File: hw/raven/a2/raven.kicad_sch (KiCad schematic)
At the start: 79 parts, among them J101 Pinhdr_01x02, J102 Pinhdr_01x03, J103 JTAG IN, J104 Pinhdr_01x03, J105 Pinhdr_01x03, SW101 SW_Push, U101 74LS148, U102 74AHC157, U103 SN74LVCH16245, U104 MC68150, U105 CY2308, U106 SN74LVCH16245, U107 MC68060, U108 ATF1508, X101 48Mhz (3.3V)

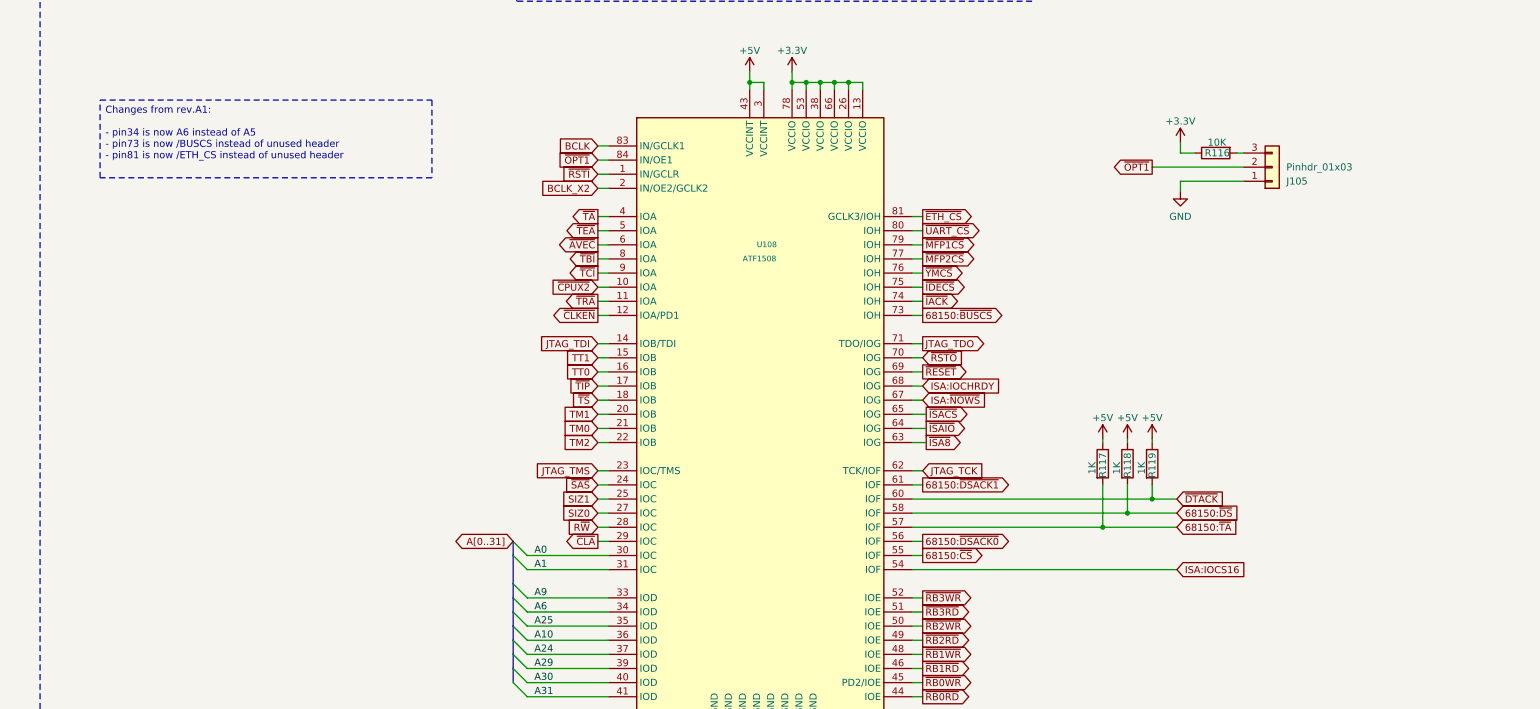
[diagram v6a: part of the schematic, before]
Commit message: ISA:MEMCS16 for 8bit support
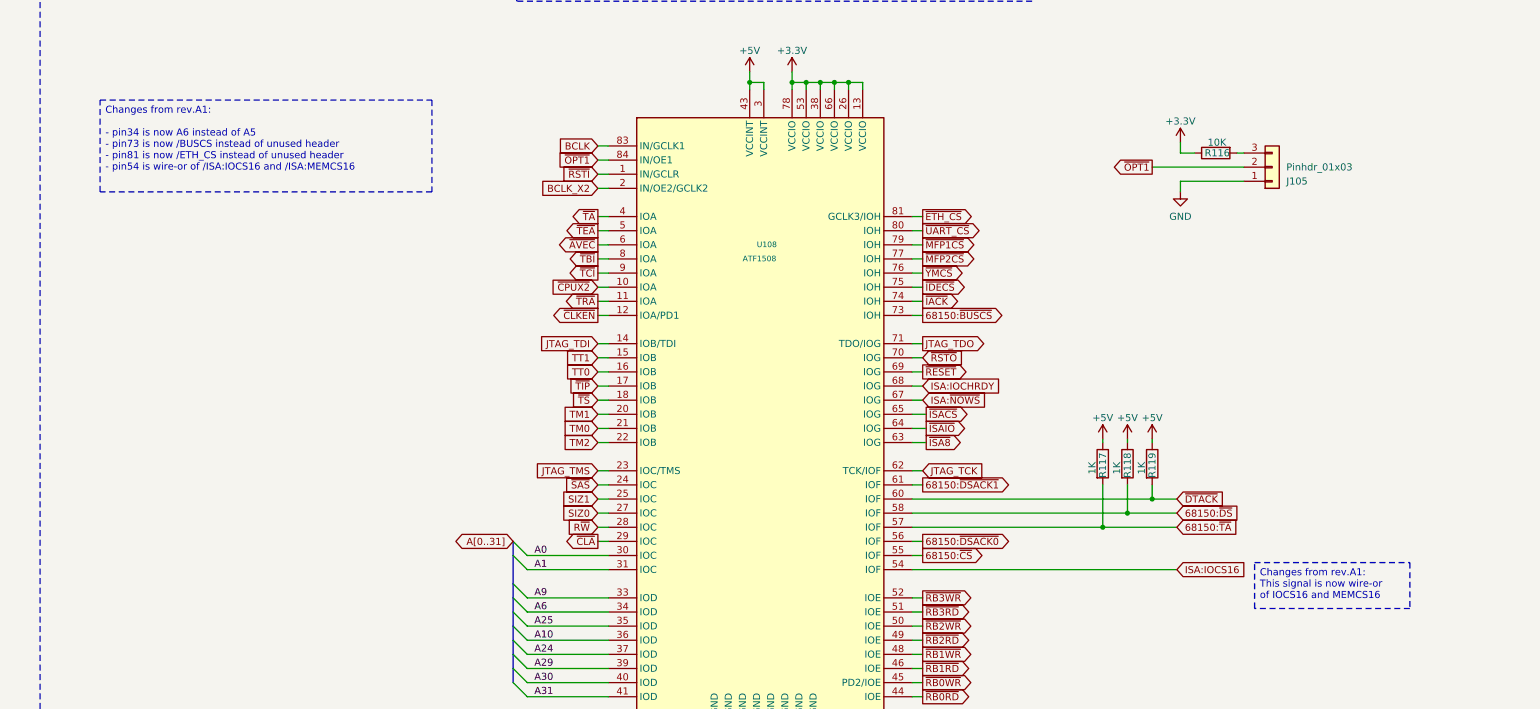
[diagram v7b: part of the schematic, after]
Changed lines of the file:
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@@
+		)
+	)
+	(text_box "Changes from rev.A1:\nThis signal is now wire-or of IOCS16 and MEMCS16\n"
+		(exclude_from_sim no)
+		(at 730.25 391.795 0)
+		(size 27.94 8.255)
+		(margins 0.9525 0.9525 0.9525 0.9525)
+		(stroke
+			(width 0)
+			(type dot)
+		)
+		(fill
+			(type none)
+		)
+		(effects
+			(font
+				(size 1.27 1.27)
+			)
+			(justify left top)
 		)
 	)
@@
 		)
 	)
-	(text_box "Changes from rev.A1:\n\n- pin34 is now A6 instead of A5\n- pin73 is now /BUSCS instead of unused header\n- pin81 is now /ETH_CS instead of unused header"
+	(text_box "Changes from rev.A1:\n\n- pin34 is now A6 instead of A5\n- pin73 is now /BUSCS instead of unused header\n- pin81 is now /ETH_CS instead of unused header\n- pin54 is wire-or of /ISA:IOCS16 and /ISA:MEMCS16"
 		(exclude_from_sim no)
 		(at 522.605 308.61 0)
-		(size 59.69 13.97)
+		(size 59.69 16.51)
 		(margins 0.9525 0.9525 0.9525 0.9525)
 		(stroke
